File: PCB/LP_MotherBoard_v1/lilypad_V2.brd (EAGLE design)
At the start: 63.5 x 53.3 mm, 30 parts, among them U2 INA169, X4 BQ24074

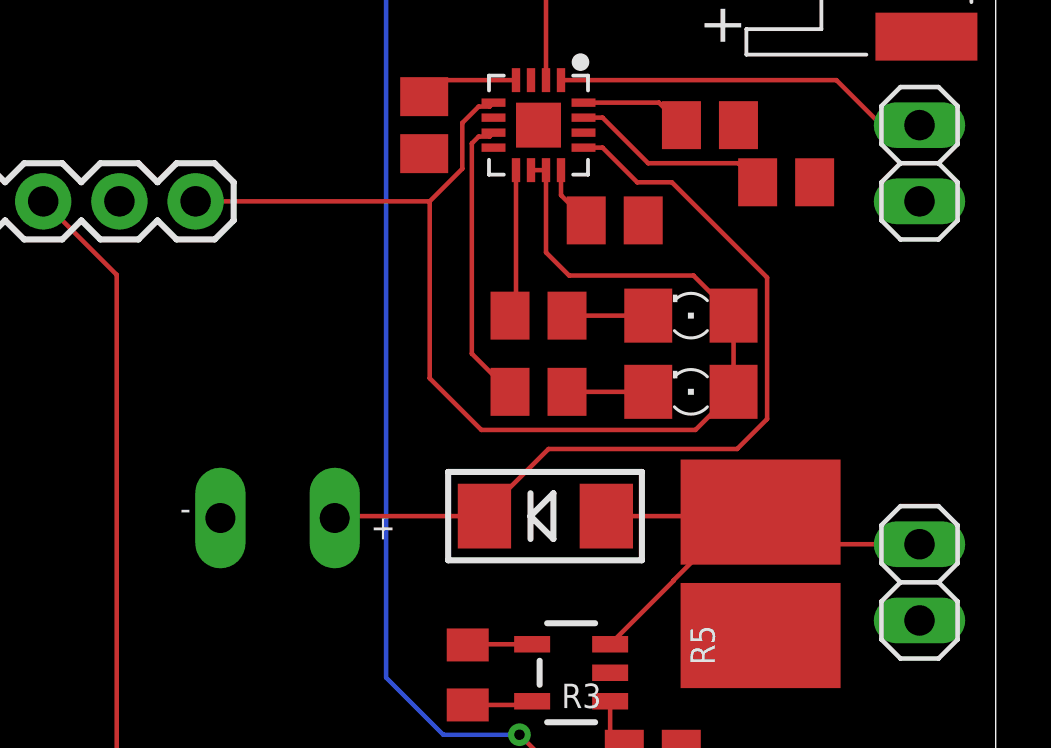
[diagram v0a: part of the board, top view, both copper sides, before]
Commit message: Fixed some sch errors
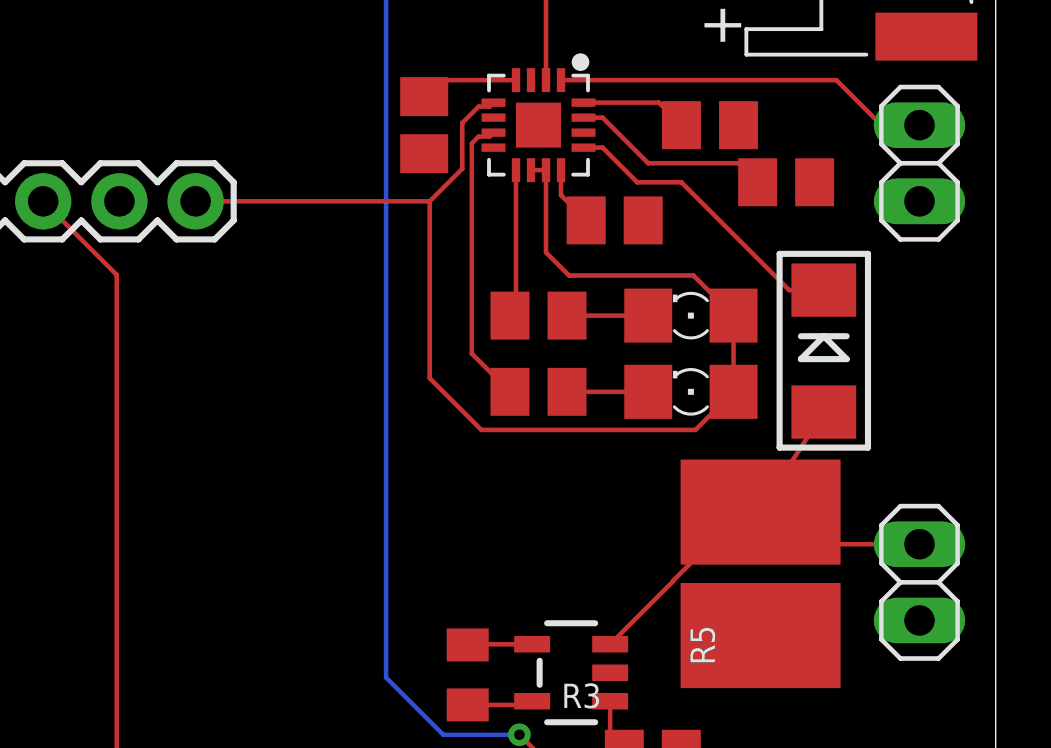
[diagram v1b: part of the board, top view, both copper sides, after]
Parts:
- removed +, -: (no value), microbuilder:1X01_OVAL
- moved D2 10.8 mm to (57.8, 19.1), turned to 270 degrees
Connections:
- net GND: no longer -.1
- net N$2: no longer +.1
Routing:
- net N$2: track 28.5 -> 9.98 mm
- net CHARGER_IN: track 17.8 -> 16.9 mm
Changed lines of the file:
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@@
 <element name="C5" library="adafruit" library_urn="urn:adsk.eagle:library:420" package="C0805K" package3d_urn="urn:adsk.eagle:package:6240397/1" value="10uF" x="49.53" y="33.02" smashed="yes" rot="R90"/>
 <element name="C6" library="adafruit" library_urn="urn:adsk.eagle:library:420" package="C0805K" package3d_urn="urn:adsk.eagle:package:6240397/1" value="10uF" x="52.07" y="33.02" smashed="yes" rot="R90"/>
-<element name="D2" library="microbuilder" package="SMADIODE" value="SK34A" x="48.502" y="13.637" smashed="yes"/>
+<element name="D2" library="microbuilder" package="SMADIODE" value="SK34A" x="57.7695" y="19.1255" smashed="yes" rot="R270"/>
 <element name="HP1" library="SparkFun-Connectors" library_urn="urn:adsk.eagle:library:513" package="1X16" package3d_urn="urn:adsk.eagle:package:38258/1" value="" x="46.99" y="44.45" smashed="yes" rot="R180">
 <attribute name="VALUE" x="48.26" y="46.482" size="0.6096" layer="27" font="vector" ratio="20" rot="R180"/>
@@
 <attribute name="PROD_ID" value="CONN-09696" x="-50.8" y="-21.59" size="1.778" layer="27" rot="R270" display="off"/>
 <attribute name="VALUE" x="-0.635" y="35.56" size="1.27" layer="27" rot="R270"/>
-</element>
-<element name="-" library="microbuilder" package="1X01_OVAL" value="" x="37.656" y="13.574" smashed="yes">
-<attribute name="NAME" x="36.3098" y="13.4978" size="0.8128" layer="25" ratio="18"/>
-<attribute name="VALUE" x="36.386" y="10.399" size="0.4064" layer="27" ratio="10"/>
-</element>
-<element name="+" library="microbuilder" package="1X01_OVAL" value="" x="41.466" y="13.574" smashed="yes">
-<attribute name="NAME" x="42.6598" y="12.8628" size="0.8128" layer="25" ratio="18"/>
-<attribute name="VALUE" x="40.196" y="10.399" size="0.4064" layer="27" ratio="10"/>
 </element>
 <element name="JP7" library="adafruit" library_urn="urn:adsk.eagle:library:420" package="1X03" package3d_urn="urn:adsk.eagle:package:6240710/1" value="" x="2.54" y="40.64" smashed="yes" rot="R90">
@@
 <signals>
 <signal name="GND">
-<contactref element="-" pad="1"/>
 <contactref element="BATT" pad="2"/>
 <contactref element="X4" pad="8"/>
@@
 <vertex x="-1.27" y="-1.905"/>
 </polygon>
-<wire x1="49.76" y1="26.42" x2="48.26" y2="26.67" width="0" layer="19" extent="1-1"/>
+<wire x1="39.37" y1="44.45" x2="45.63" y2="50.73" width="0" layer="19" extent="1-1"/>
+<wire x1="49.53" y1="34.02" x2="39.37" y2="44.45" width="0" layer="19" extent="1-1"/>
+<wire x1="52.07" y1="34.02" x2="49.53" y2="34.02" width="0" layer="19" extent="1-1"/>
+<wire x1="55.99" y1="34.02" x2="52.07" y2="34.02" width="0" layer="19" extent="1-1"/>
+<wire x1="54.925" y1="26.67" x2="55.99" y2="34.02" width="0" layer="19" extent="1-1"/>
+<wire x1="57.465" y1="24.765" x2="54.925" y2="26.67" width="0" layer="19" extent="1-1"/>
+<wire x1="60.96" y1="24.13" x2="57.465" y2="24.765" width="0" layer="19" extent="1-1"/>
+<wire x1="51.75" y1="23.495" x2="54.925" y2="26.67" width="0" layer="19" extent="1-1"/>
+<wire x1="49.76" y1="26.42" x2="51.75" y2="23.495" width="0" layer="19" extent="1-1"/>
+<wire x1="48.26" y1="26.67" x2="49.76" y2="26.42" width="0" layer="19" extent="1-1"/>
 <wire x1="46.76" y1="26.92" x2="48.26" y2="26.67" width="0" layer="19" extent="1-1"/>
 <wire x1="46.76" y1="25.92" x2="46.76" y2="26.92" width="0" layer="19" extent="1-1"/>
 <wire x1="44.45" y1="25.72" x2="46.76" y2="25.92" width="0" layer="19" extent="1-1"/>
-<wire x1="51.75" y1="23.495" x2="49.76" y2="26.42" width="0" layer="19" extent="1-1"/>
-<wire x1="54.925" y1="26.67" x2="51.75" y2="23.495" width="0" layer="19" extent="1-1"/>
+<wire x1="60.96" y1="10.16" x2="60.96" y2="24.13" width="0" layer="19" extent="1-1"/>
+<wire x1="55.663" y1="9.6566" x2="60.96" y2="10.16" width="0" layer="19" extent="1-1"/>
+<wire x1="53.02" y1="5.715" x2="55.663" y2="9.6566" width="0" layer="19" extent="1-1"/>
+<wire x1="50.6481" y1="8.416" x2="53.02" y2="5.715" width="0" layer="19" extent="1-1"/>
+<wire x1="48.0479" y1="9.366" x2="50.6481" y2="8.416" width="0" layer="19" extent="1-1"/>
+<wire x1="31.66" y1="2.47" x2="45.901" y2="9.343" width="0" layer="19" extent="1-1"/>
+<wire x1="2.54" y1="43.18" x2="39.37" y2="44.45" width="0" layer="19" extent="1-1"/>
+<wire x1="2.54" y1="31.75" x2="2.54" y2="43.18" width="0" layer="19" extent="1-1"/>
 </signal>
 <signal name="THERM">
@@
 <wire x1="55.6722" y1="13.7622" x2="55.663" y2="13.7714" width="0.1524" layer="1"/>
 <wire x1="55.663" y1="13.7714" x2="55.5286" y2="13.637" width="0.1524" layer="1"/>
-<wire x1="55.5286" y1="13.637" x2="50.5213" y2="13.637" width="0.1524" layer="1"/>
+<wire x1="55.5286" y1="13.637" x2="57.7695" y2="17.1062" width="0.1524" layer="1"/>
 <wire x1="50.6481" y1="9.366" x2="52.7674" y2="11.4853" width="0.1524" layer="1"/>
 <wire x1="52.7674" y1="11.4853" x2="52.7674" y2="11.5038875" width="0.1524" layer="1"/>
@@
 <contactref element="X4" pad="13"/>
 <contactref element="D2" pad="C"/>
-<contactref element="+" pad="1"/>
-<wire x1="46.4573" y1="13.637" x2="46.355" y2="13.637" width="0.1524" layer="1"/>
-<wire x1="46.355" y1="13.637" x2="41.529" y2="13.637" width="0.1524" layer="1"/>
-<wire x1="41.529" y1="13.637" x2="41.466" y2="13.574" width="0.1524" layer="1"/>
 <wire x1="49.76" y1="25.92" x2="50.395" y2="25.92" width="0.1524" layer="1"/>
 <wire x1="51.55" y1="24.765" x2="50.395" y2="25.92" width="0.1524" layer="1"/>
-<wire x1="51.55" y1="24.765" x2="52.705" y2="24.765" width="0.1524" layer="1"/>
-<wire x1="52.705" y1="24.765" x2="55.88" y2="21.59" width="0.1524" layer="1"/>
-<wire x1="55.88" y1="16.8732125" x2="54.8817875" y2="15.875" width="0.1524" layer="1"/>
-<wire x1="48.593" y1="15.875" x2="46.355" y2="13.637" width="0.1524" layer="1"/>
-<wire x1="55.88" y1="21.59" x2="55.88" y2="16.8732125" width="0.1524" layer="1"/>
-<wire x1="54.8817875" y1="15.875" x2="48.593" y2="15.875" width="0.1524" layer="1"/>
+<wire x1="51.55" y1="24.765" x2="53.0225" y2="24.765" width="0.1524" layer="1"/>
+<wire x1="56.6173" y1="21.1702" x2="57.7695" y2="21.1702" width="0.1524" layer="1"/>
+<wire x1="53.0225" y1="24.765" x2="56.6173" y2="21.1702" width="0.1524" layer="1"/>
 </signal>
 <signal name="N$3">

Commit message: Lilypad PCB Post Review and README
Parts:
- added J2: (no value), SparkFun-Connectors:1X04
- added JP1: (no value), adafruit:1X03
- moved C1 6.03 mm to (45.9, 14.4)
- moved U2 6.03 mm to (49.3, 14.4)
- moved R3 5.97 mm to (49.5, 11.1)
- moved J1 2.22 mm to (4.76, 34.3)
- moved JP7 2.22 mm to (4.76, 40.6)
- moved R1 0.32 mm to (50.8, 23.2)
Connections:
- new net VIN: HP2.1, JP1.2
- net GND: now also J2.2
- net SCL: now also J2.3
- net SDA: now also J2.4
- net VBAT: now also JP1.3; no longer HP2.1
- net VCC: now also J2.1
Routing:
- net VBAT: track 42.6 -> 54.3 mm, vias 0 -> 1
- net VIN: track 0.00 -> 11.4 mm
- net SDA: track 7.40 -> 16.1 mm
- net SCL: track 11.0 -> 19.7 mm
- net A1: track 50.8 -> 44.9 mm, vias 1 -> 0
- net GND: track 2.16 -> 7.17 mm
- net CHARGER_IN: track 16.9 -> 21.0 mm
- net TMP_PRB: track 9.94 -> 7.71 mm
- net VCC: track 2.20 -> 3.98 mm, vias 0 -> 1
- net RX: vias 2 -> 0
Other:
- board size 63.5 x 53.3 mm -> 61 x 53.7 mm
- board text added: "Lilypad v2"
